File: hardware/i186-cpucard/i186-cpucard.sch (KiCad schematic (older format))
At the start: 49 parts, among them K1 CONN_3, P1 CONN_4, P10 CONN_4, P11 CONN_4, P12 CONN_4X2, P13 CONN_2X2, P14 CONN_4, P15 CONN_4, P16 CONN_4, P17 CONN_4, P18 CONN_4, P19 CONN_4, P2 CONN_4, P20 CONN_4, P21 CONN_4, P22 CONN_4, P3 CONN_4, P4 CONN_4, P5 CONN_4, P6 CONN_2X2, P7 CONN_4, P8 CONN_2X2, P9 CONN_4, U1 74LS574, U2 74LS574, U3 74LS574, U4 74LS574, U5 I80186, U6 74LS574, U7 74HC245, U8 74HC245, U9 74HC245

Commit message: ficzes
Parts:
- added U10: 74HC14, symbol 74HC14
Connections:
- net GND: now also U10.3, U10.5, U10.7 (GND), U10.7 (GND), U10.7 (GND), U10.7 (GND), U10.7 (GND), U10.7 (GND)
- net VCC: now also U10.11, U10.13, U10.14 (VCC), U10.14 (VCC), U10.14 (VCC), U10.14 (VCC), U10.14 (VCC), U10.14 (VCC), U10.9
- net bus enable: now also U10.1; no longer U5.55 (ARDY)
- new net: U10.2, U5.55 (ARDY)
- no-connect marks 42 -> 47

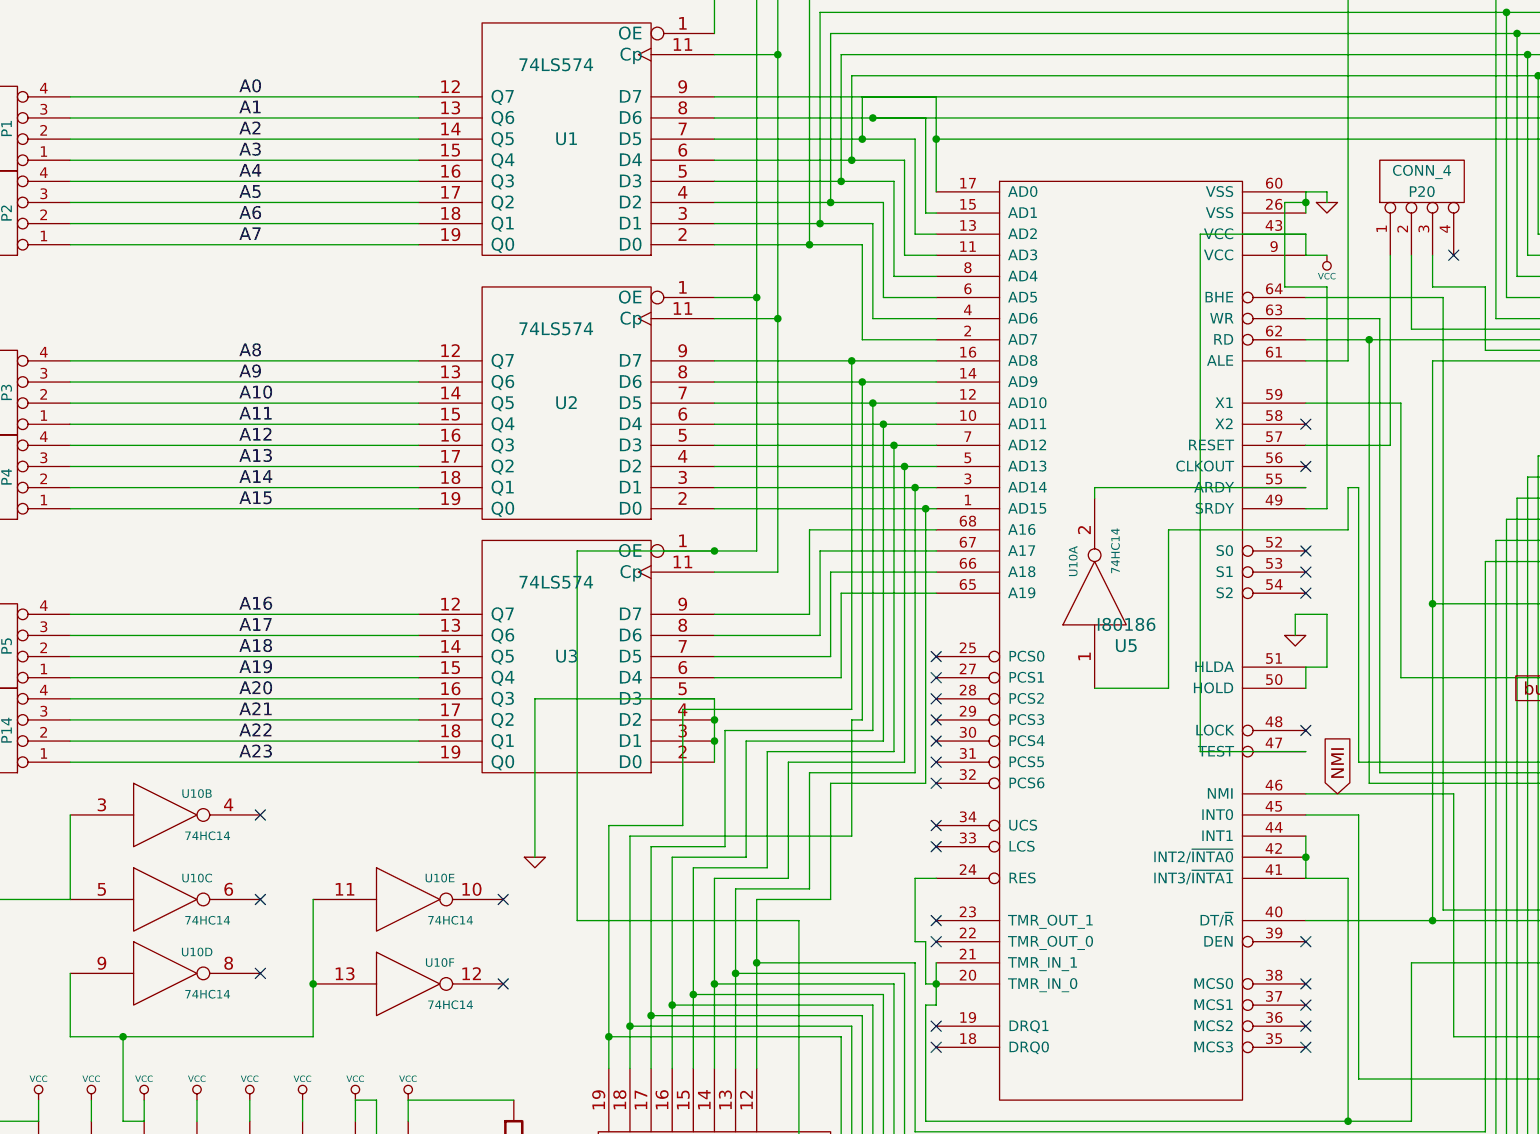
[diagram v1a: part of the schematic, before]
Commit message: fixed broken reset
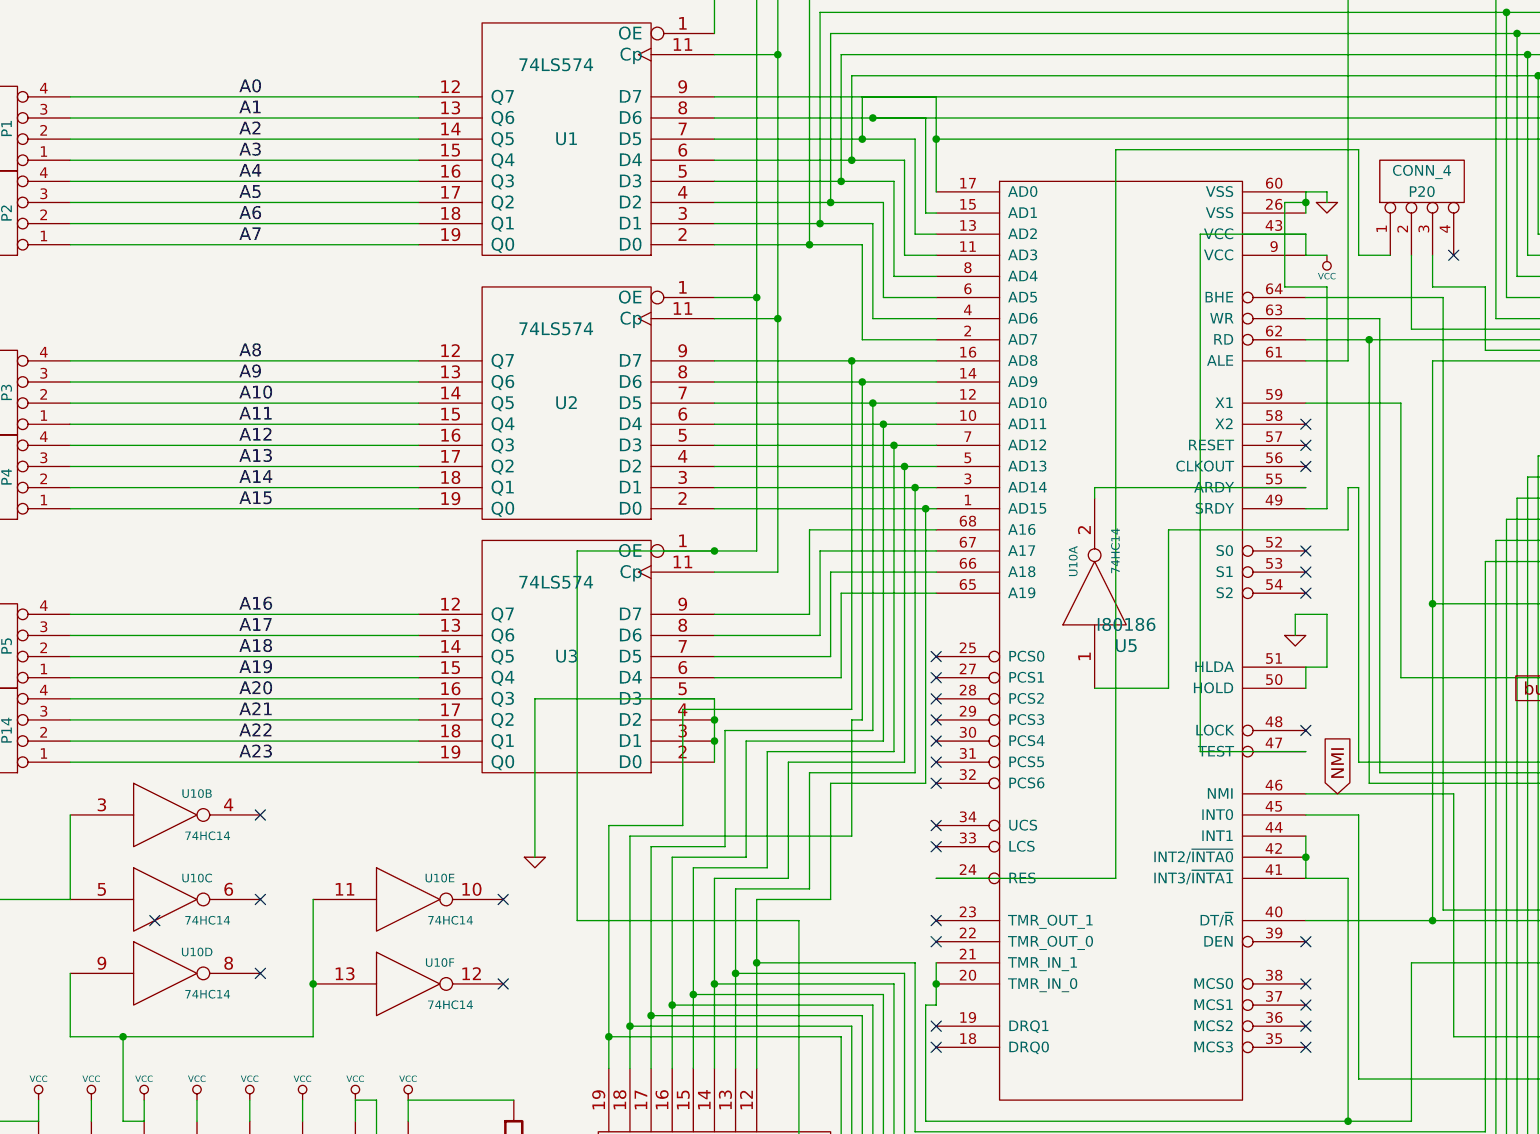
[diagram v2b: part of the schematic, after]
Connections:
- net GND: no longer U5.24 (RES)
- net at P20.1 (P1): now also U5.24 (RES); no longer U5.57 (RESET)
- no-connect marks 47 -> 49
